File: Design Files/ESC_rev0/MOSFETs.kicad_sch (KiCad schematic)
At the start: 34 parts, among them J4 WP-BUTR, J5 WP-BUTR, J6 WP-BUTR, Q1 HSBA15810C, Q2 HSBA15810C, Q3 HSBA15810C, Q4 HSBA15810C, Q5 HSBA15810C, Q6 HSBA15810C

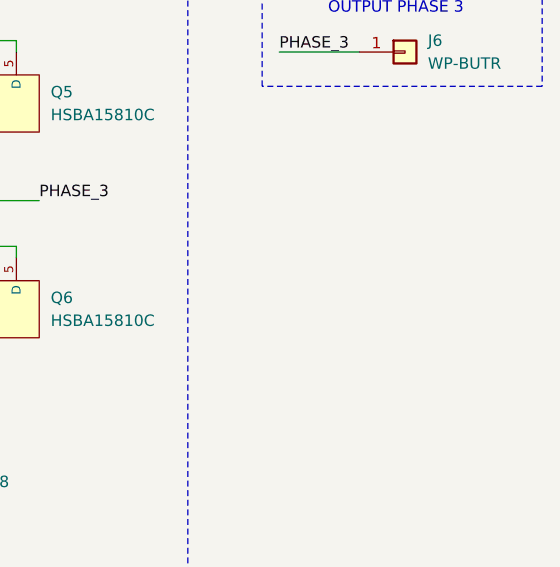
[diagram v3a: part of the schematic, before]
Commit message: update 13
assigned all footprints (provisionally) and imported them - errors and warning occurred, must be corrected in the future
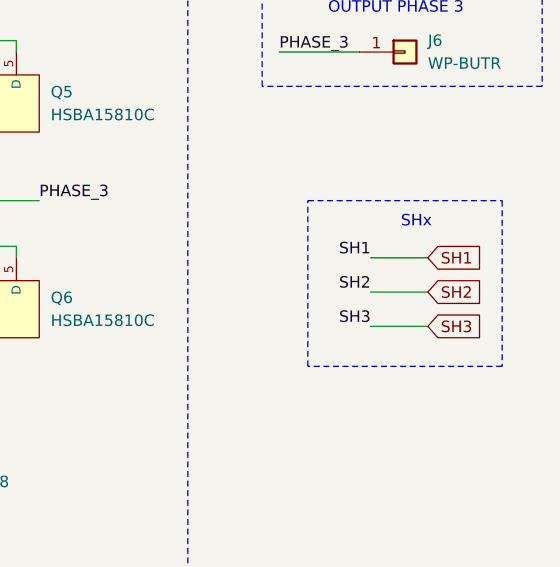
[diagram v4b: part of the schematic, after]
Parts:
- NT1, NT2, NT3, NT4, NT5, NT6, NT7, NT8: footprint (none) -> NetTie:NetTie-2_SMD_Pad2.0mm
- Q1, Q2, Q3, Q4, Q5, Q6: footprint footprint:PQFN-8_L6.0-W5.0-P1.27-LS6.0-BL -> HSBA15810C_foot:PQFN-8_L6.0-W5.0-P1.27-LS6.0-BL
- R27, R28, R29, R30, R31, R32, R33, R34, R35, R36, R37, R38, R39, R40, R41: footprint (none) -> Resistor_SMD:R_0603_1608Metric
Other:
- note added: "SHx"
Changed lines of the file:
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@@
 	(wire
 		(pts
+			(xy 264.16 97.79) (xy 257.81 97.79)
+		)
+		(stroke
+			(width 0)
+			(type default)
+		)
+	)
+	(wire
+		(pts
 			(xy 210.82 96.52) (xy 208.28 96.52)
 		)
@@
 	(wire
 		(pts
+			(xy 264.16 101.6) (xy 257.81 101.6)
+		)
+		(stroke
+			(width 0)
+			(type default)
+		)
+	)
+	(wire
+		(pts
 			(xy 149.86 96.52) (xy 149.86 97.79)
 		)
@@
 	(wire
 		(pts
+			(xy 264.16 105.41) (xy 257.81 105.41)
+		)
+		(stroke
+			(width 0)
+			(type default)
+		)
+	)
+	(wire
+		(pts
 			(xy 149.86 87.63) (xy 149.86 86.36)
 		)
@@
 	)
 	(rectangle
+		(start 250.825 91.44)
+		(end 272.415 109.855)
+		(stroke
+			(width 0)
+			(type dash)
+		)
+		(fill
+			(type none)
+		)
+	)
+	(rectangle
 		(start 245.745 42.545)
 		(end 276.86 53.34)
@@
 		)
 	)
+	(text "SHx"
+		(exclude_from_sim no)
+		(at 262.89 93.853 0)
+		(effects
+			(font
+				(size 1.27 1.27)
+			)
+		)
+	)
 	(text "PHASE 1"
 		(exclude_from_sim no)
@@
 		)
 	)
+	(label "SH2"
+		(at 257.81 101.6 180)
+		(fields_autoplaced yes)
+		(effects
+			(font
+				(size 1.27 1.27)
+			)
+			(justify right bottom)
+		)
+	)
 	(label "S1_P"
 		(at 71.12 132.08 0)
@@
 		)
 	)
+	(label "SH1"
+		(at 257.81 97.79 180)
+		(fields_autoplaced yes)
+		(effects
+			(font
+				(size 1.27 1.27)
+			)
+			(justify right bottom)
+		)
+	)
 	(label "GL1"
 		(at 49.53 104.14 0)
@@
 		)
 	)
+	(label "SH3"
+		(at 257.81 105.41 180)
+		(fields_autoplaced yes)
+		(effects
+			(font
+				(size 1.27 1.27)
+			)
+			(justify right bottom)
+		)
+	)
 	(label "SN1"
 		(at 31.75 113.03 0)
@@
 		)
 	)
+	(global_label "SH1"
+		(shape input)
+		(at 264.16 97.79 0)
+		(fields_autoplaced yes)
+		(effects
+			(font
+				(size 1.27 1.27)
+			)
+			(justify left)
+		)
+		(property "Intersheetrefs" "${INTERSHEET_REFS}"
+			(at 270.8947 97.79 0)
+			(effects
+				(font
+					(size 1.27 1.27)
+				)
+				(justify left)
+				(hide yes)
+			)
+		)
+	)
 	(global_label "M_H1"
 		(shape input)
@@
 		)
 	)
+	(global_label "SH3"
+		(shape input)
+		(at 264.16 105.41 0)
+		(fields_autoplaced yes)
+		(effects
+			(font
+				(size 1.27 1.27)
+			)
+			(justify left)
+		)
+		(property "Intersheetrefs" "${INTERSHEET_REFS}"
+			(at 270.8947 105.41 0)
+			(effects
+				(font
+					(size 1.27 1.27)
+				)
+				(justify left)
+				(hide yes)
+			)
+		)
+	)
 	(global_label "M_L3"
 		(shape input)
@@
 		)
 	)
+	(global_label "SH2"
+		(shape input)
+		(at 264.16 101.6 0)
+		(fields_autoplaced yes)
+		(effects
+			(font
+				(size 1.27 1.27)
+			)
+			(justify left)
+		)
+		(property "Intersheetrefs" "${INTERSHEET_REFS}"
+			(at 270.8947 101.6 0)
+			(effects
+				(font
+					(size 1.27 1.27)
+				)
+				(justify left)
+				(hide yes)
+			)
+		)
+	)
 	(global_label "M_L1"
 		(shape input)
@@
 			)
 		)
-		(property "Footprint" ""
+		(property "Footprint" "Resistor_SMD:R_0603_1608Metric"
 			(at 83.058 134.62 90)
 			(effects
@@
 			)
 		)
-		(property "Footprint" "footprint:PQFN-8_L6.0-W5.0-P1.27-LS6.0-BL"
+		(property "Footprint" "HSBA15810C_foot:PQFN-8_L6.0-W5.0-P1.27-LS6.0-BL"
 			(at 216.408 65.786 0)
 			(effects
@@
 			)
 		)
-		(property "Footprint" ""
+		(property "Footprint" "NetTie:NetTie-2_SMD_Pad2.0mm"
 			(at 205.74 91.44 0)
 			(effects
@@
 			)
 		)
-		(property "Footprint" ""
+		(property "Footprint" "Resistor_SMD:R_0603_1608Metric"
 			(at 60.96 131.318 90)
 			(effects
@@
 			)
 		)
-		(property "Footprint" ""
+		(property "Footprint" "Resistor_SMD:R_0603_1608Metric"
 			(at 125.73 105.918 90)
 			(effects
@@
 			)
 		)
-		(property "Footprint" ""
+		(property "Footprint" "Resistor_SMD:R_0603_1608Metric"
 			(at 125.73 83.058 90)
 			(effects
@@
 			)
 		)
-		(property "Footprint" ""
+		(property "Footprint" "NetTie:NetTie-2_SMD_Pad2.0mm"
 			(at 213.36 121.92 0)
 			(effects
@@
 			)
 		)
-		(property "Footprint" ""
+		(property "Footprint" "Resistor_SMD:R_0603_1608Metric"
 			(at 197.612 109.22 90)
 			(effects
@@
 			)
 		)
-		(property "Footprint" ""
+		(property "Footprint" "NetTie:NetTie-2_SMD_Pad2.0mm"
 			(at 73.66 91.44 0)
 			(effects
@@
 			)
 		)
-		(property "Footprint" ""
+		(property "Footprint" "Resistor_SMD:R_0603_1608Metric"
 			(at 60.96 141.478 90)
 			(effects
@@
 			)
 		)
-		(property "Footprint" ""
+		(property "Footprint" "Resistor_SMD:R_0603_1608Metric"
 			(at 191.77 83.058 90)
 			(effects
@@
 			)
 		)
-		(property "Footprint" ""
+		(property "Footprint" "NetTie:NetTie-2_SMD_Pad2.0mm"
 			(at 81.28 144.78 0)
 			(effects
@@
 			)
 		)
-		(property "Footprint" "footprint:PQFN-8_L6.0-W5.0-P1.27-LS6.0-BL"
+		(property "Footprint" "HSBA15810C_foot:PQFN-8_L6.0-W5.0-P1.27-LS6.0-BL"
 			(at 84.328 65.786 0)
 			(effects
@@
 			)
 		)
-		(property "Footprint" "footprint:PQFN-8_L6.0-W5.0-P1.27-LS6.0-BL"
+		(property "Footprint" "HSBA15810C_foot:PQFN-8_L6.0-W5.0-P1.27-LS6.0-BL"
 			(at 84.328 88.646 0)
 			(effects
@@
 			)
 		)
-		(property "Footprint" ""
+		(property "Footprint" "Resistor_SMD:R_0603_1608Metric"
 			(at 131.572 109.22 90)
 			(effects
@@
 			)
 		)
-		(property "Footprint" ""
+		(property "Footprint" "Resistor_SMD:R_0603_1608Metric"
 			(at 191.77 105.918 90)
 			(effects
@@
 			)
 		)
-		(property "Footprint" ""
+		(property "Footprint" "NetTie:NetTie-2_SMD_Pad2.0mm"
 			(at 147.32 121.92 0)
 			(effects
@@
 			)
 		)
-		(property "Footprint" "footprint:PQFN-8_L6.0-W5.0-P1.27-LS6.0-BL"
+		(property "Footprint" "HSBA15810C_foot:PQFN-8_L6.0-W5.0-P1.27-LS6.0-BL"
 			(at 150.368 65.786 0)
 			(effects
@@
 			)
 		)
-		(property "Footprint" ""
+		(property "Footprint" "Resistor_SMD:R_0603_1608Metric"
 			(at 149.098 134.62 90)
 			(effects
@@
 			)
 		)
-		(property "Footprint" ""
+		(property "Footprint" "Resistor_SMD:R_0603_1608Metric"
 			(at 59.69 105.918 90)
 			(effects
@@
 			)
 		)
-		(property "Footprint" ""
+		(property "Footprint" "NetTie:NetTie-2_SMD_Pad2.0mm"
 			(at 147.32 144.78 0)
 			(effects
@@
 			)
 		)
-		(property "Footprint" ""
+		(property "Footprint" "Resistor_SMD:R_0603_1608Metric"
 			(at 127 141.478 90)
 			(effects
@@
 			)
 		)
-		(property "Footprint" ""
+		(property "Footprint" "NetTie:NetTie-2_SMD_Pad2.0mm"
 			(at 139.7 91.44 0)
 			(effects
@@
 			)
 		)
-		(property "Footprint" ""
+		(property "Footprint" "Resistor_SMD:R_0603_1608Metric"
 			(at 59.69 83.058 90)
 			(effects
@@
 			)
 		)
-		(property "Footprint" ""
+		(property "Footprint" "Resistor_SMD:R_0603_1608Metric"
 			(at 65.532 109.22 90)
 			(effects
@@
 			)
 		)
-		(property "Footprint" ""
+		(property "Footprint" "NetTie:NetTie-2_SMD_Pad2.0mm"
 			(at 81.28 121.92 0)
 			(effects
@@
 			)
 		)
-		(property "Footprint" "footprint:PQFN-8_L6.0-W5.0-P1.27-LS6.0-BL"
+		(property "Footprint" "HSBA15810C_foot:PQFN-8_L6.0-W5.0-P1.27-LS6.0-BL"
 			(at 216.408 88.646 0)
 			(effects
@@
 			)
 		)
-		(property "Footprint" "footprint:PQFN-8_L6.0-W5.0-P1.27-LS6.0-BL"
+		(property "Footprint" "HSBA15810C_foot:PQFN-8_L6.0-W5.0-P1.27-LS6.0-BL"
 			(at 150.368 88.646 0)
 			(effects
@@
 			)
 		)
-		(property "Footprint" ""
+		(property "Footprint" "Resistor_SMD:R_0603_1608Metric"
 			(at 127 131.318 90)
 			(effects

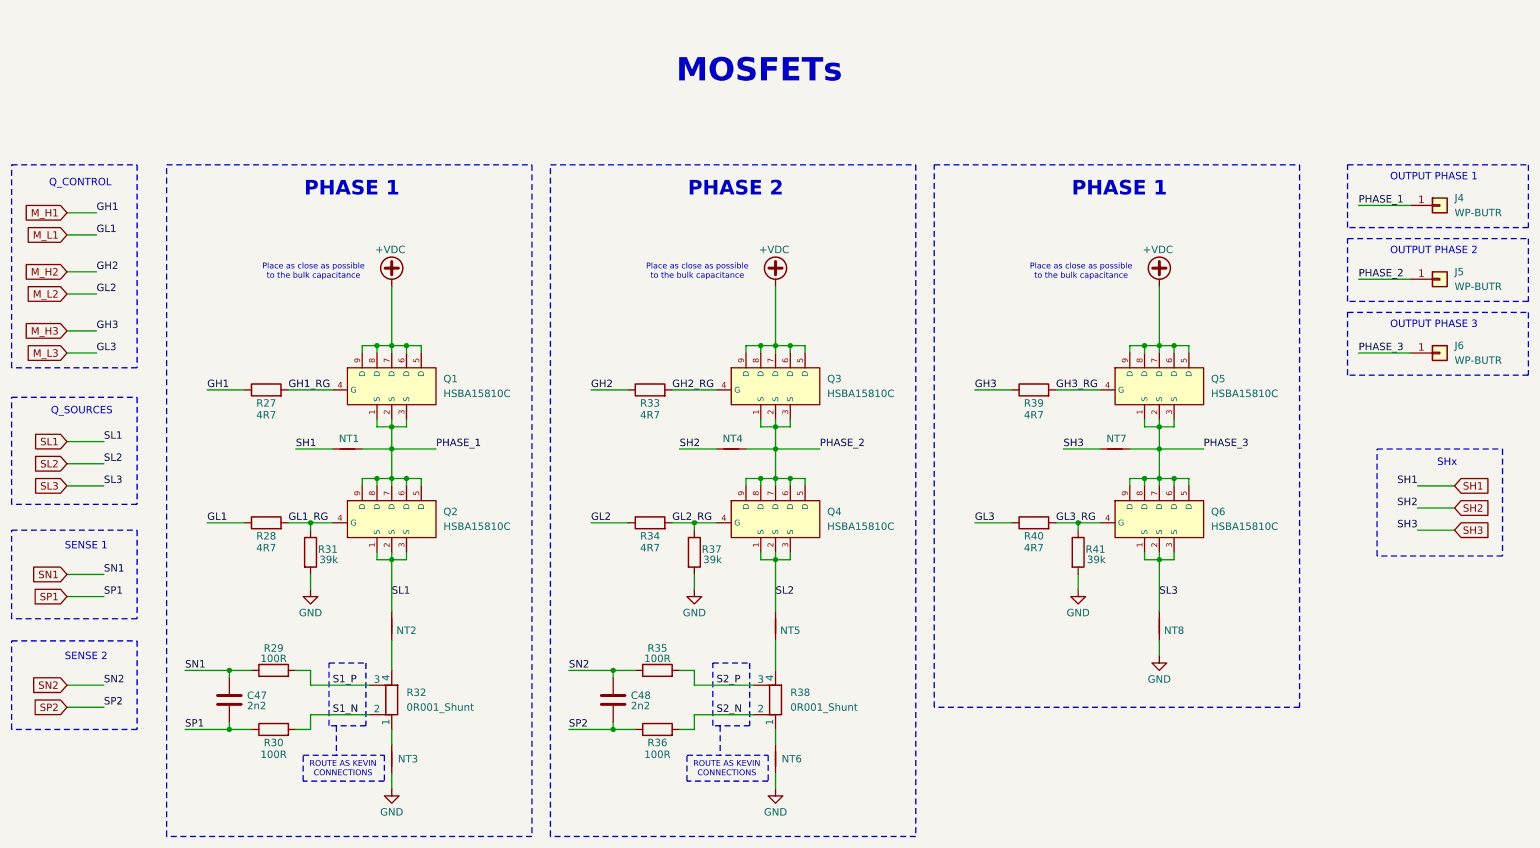
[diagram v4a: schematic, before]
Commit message: update 16
All components placed on board. Some components modifications and addition were made: added 3D models, changed some symbols and footprints positions and some component types.
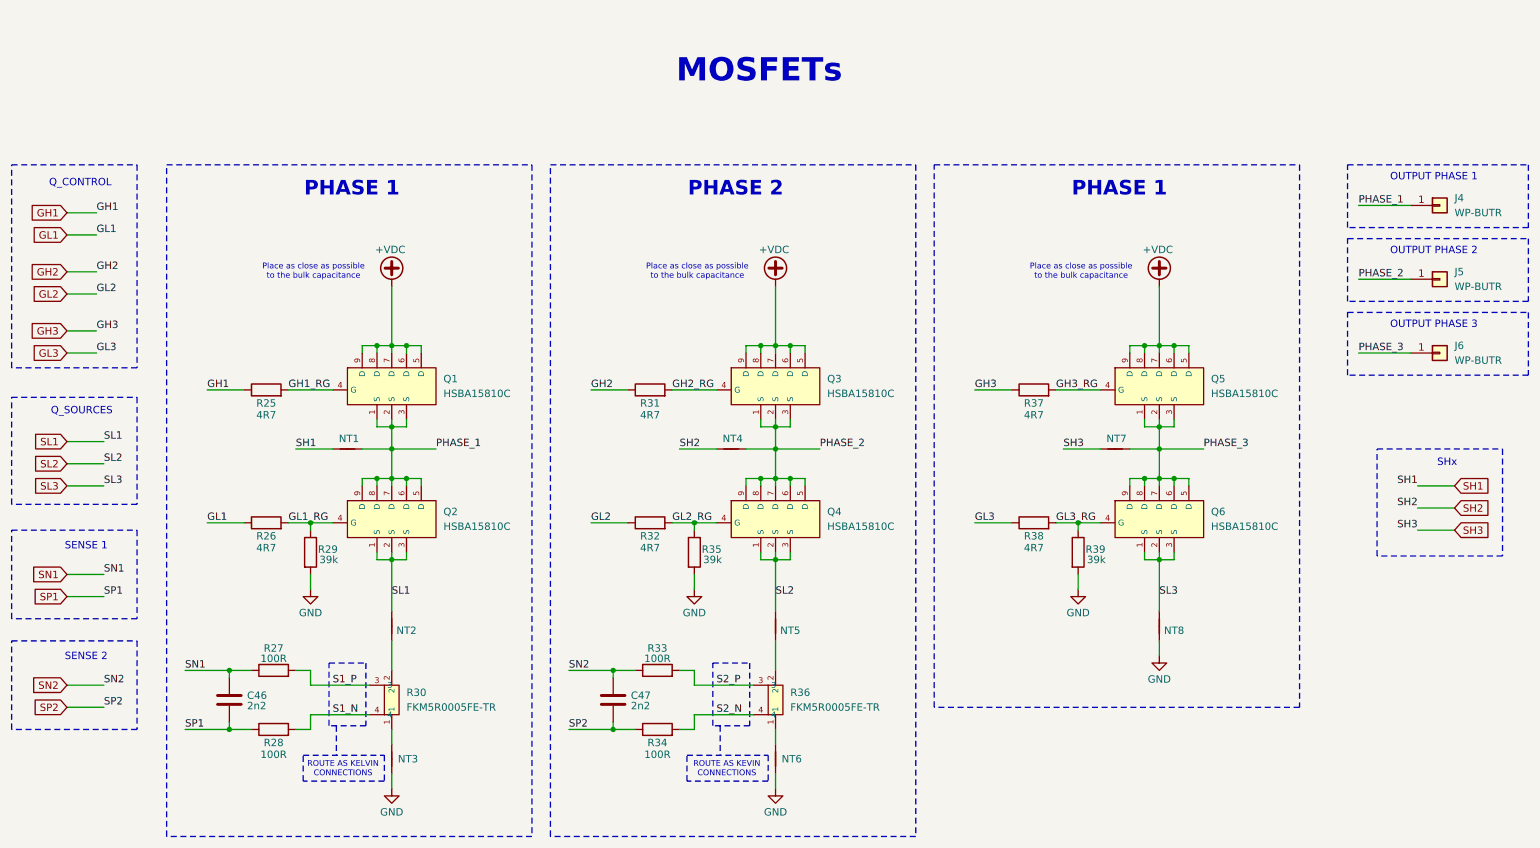
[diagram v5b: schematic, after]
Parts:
- removed R32, R38: 0R001_Shunt, Resistor_SMD:R_0603_1608Metric, symbol Device:R_Shunt
- added R30, R36: FKM5R0005FE-TR, FKM5R0005FE-TR:RES-SMD_4P-L6.9-W6.6_OHMITE_FKM5RXXXXFE-TR, symbol FKM5R0005FE-TR:FKM5R0005FE-TR
- C46: renamed from C47; footprint Capacitor_SMD:C_0201_0603Metric -> Capacitor_SMD:C_0603_1608Metric
- C47: renamed from C48; footprint Capacitor_SMD:C_0201_0603Metric -> Capacitor_SMD:C_0603_1608Metric
- NT1, NT2, NT5: footprint NetTie:NetTie-2_SMD_Pad2.0mm -> NetTie:NetTie-2_SMD_Pad2.00mm_Small
- renumbered R27 to R25, R28 to R26, R29 to R27, R30 to R28, R31 to R29, R33 to R31, R34 to R32, R35 to R33, R36 to R34, R37 to R35, R39 to R37, R40 to R38, R41 to R39
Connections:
- net S1_N: now also R30.4
- net S1_P: now also R30.3
- net S2_N: now also R36.4
- net S2_P: now also R36.3
- net at NT3.2: now also R30.1
- net at NT2.1: now also R30.2
- net at NT5.1: now also R36.2
- net at NT6.2: now also R36.1
- net M_H1 renamed GH1
- net M_H2 renamed GH2
- net M_H3 renamed GH3
- net M_L1 renamed GL1
- net M_L2 renamed GL2
- net M_L3 renamed GL3
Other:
- note added: "ROUTE AS KELVIN CONNECTIONS"
